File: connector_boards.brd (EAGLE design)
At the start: 59.9 x 46 mm, 3 parts

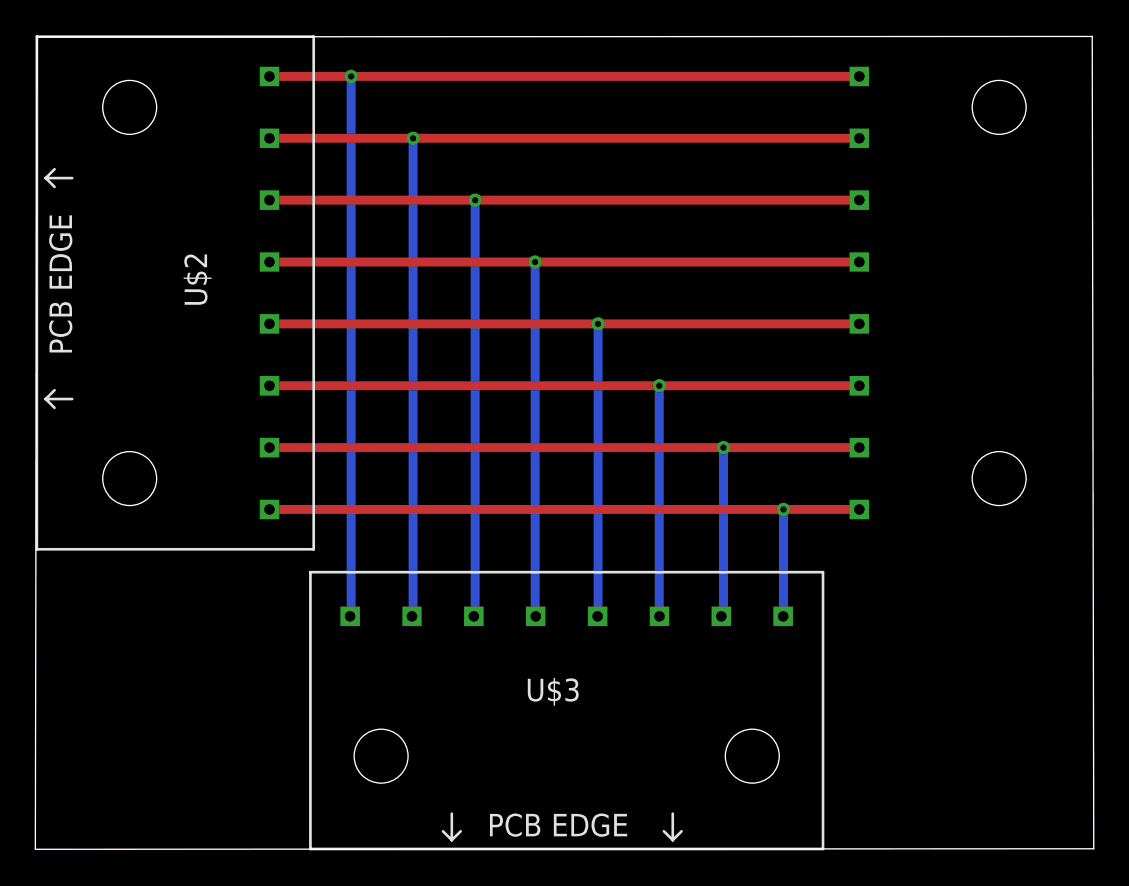
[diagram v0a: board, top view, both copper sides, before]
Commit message: Return to the original state after major disruption
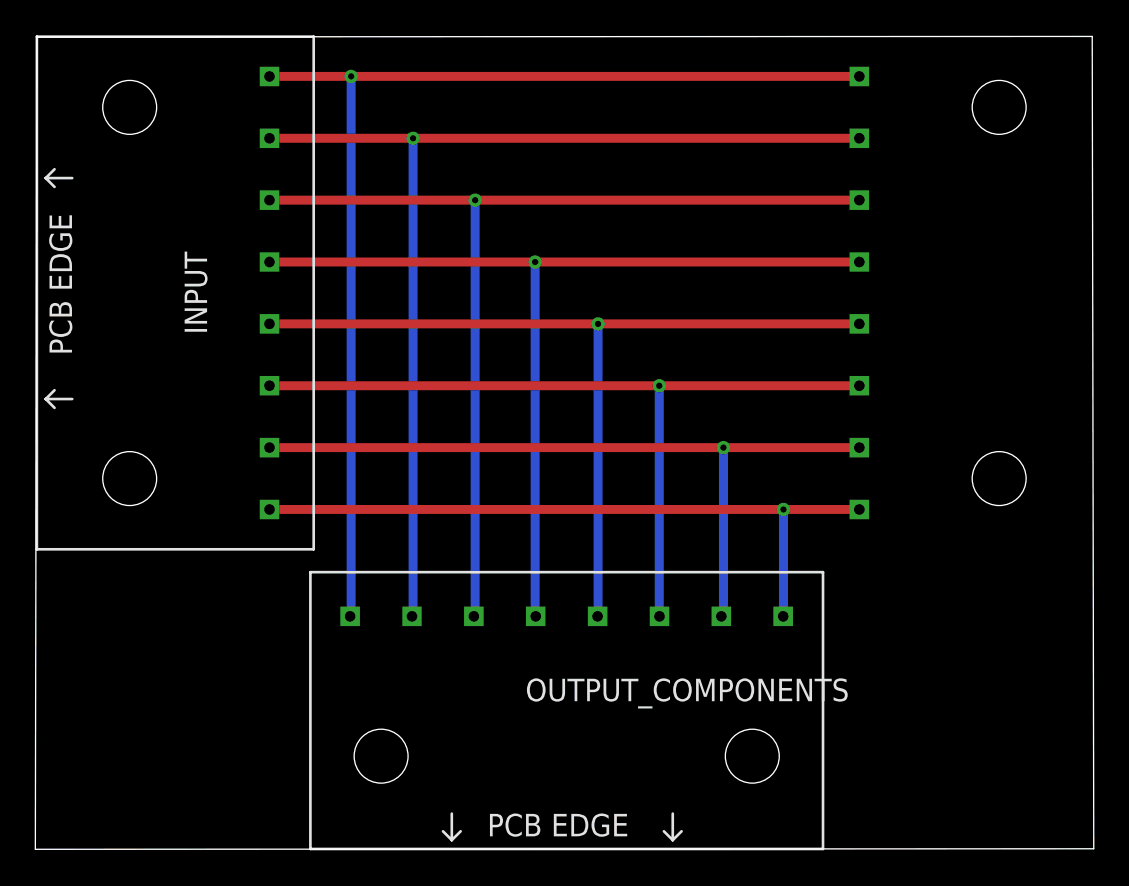
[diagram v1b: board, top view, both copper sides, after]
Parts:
- renumbered U$1 to OUTPUT, U$2 to INPUT, U$3 to OUTPUT_COMPONENTS
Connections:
- net N$1 renamed BREAK_SIG
- net N$2 renamed HAZ_L_SIG
- net N$3 renamed HAZ_R_SIG
- net N$4 renamed HEADLIGHT_SIG
- net N$5 renamed REARLIGHT_SIG
- net N$8 renamed GND
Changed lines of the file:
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@@
 <?xml version="1.0" encoding="utf-8"?>
 <!DOCTYPE eagle SYSTEM "eagle.dtd">
-<eagle version="9.1.3">
+<eagle version="9.2.2">
 <drawing>
 <settings>
@@
 </autorouter>
 <elements>
-<element name="U$1" library="master_library" package="8-PIN-MOLEX" value="8-PIN-MOLEX-RA-FEMALE" x="91.44" y="67.31" rot="MR270"/>
-<element name="U$2" library="master_library" package="8-PIN-MOLEX" value="8-PIN-MOLEX-RA-FEMALE" x="31.75" y="67.31" rot="R270"/>
-<element name="U$3" library="master_library" package="8-PIN-MOLEX" value="8-PIN-MOLEX-RA-FEMALE" x="47.224134375" y="21.35574375"/>
+<element name="OUTPUT" library="master_library" package="8-PIN-MOLEX" value="8-PIN-MOLEX-RA-FEMALE" x="91.44" y="67.31" smashed="yes" rot="MR270">
+<attribute name="NAME" x="83.080334375" y="55.148" size="1.27" layer="26" rot="MR270"/>
+</element>
+<element name="INPUT" library="master_library" package="8-PIN-MOLEX" value="8-PIN-MOLEX-RA-FEMALE" x="31.75" y="67.31" smashed="yes" rot="R270">
+<attribute name="NAME" x="40.109665625" y="55.148" size="1.27" layer="25" rot="R270"/>
+</element>
+<element name="OUTPUT_COMPONENTS" library="master_library" package="8-PIN-MOLEX" value="8-PIN-MOLEX-RA-FEMALE" x="47.224134375" y="21.35574375" smashed="yes">
+<attribute name="NAME" x="59.386134375" y="29.715409375" size="1.27" layer="25"/>
+</element>
 </elements>
 <signals>
-<signal name="N$1">
-<contactref element="U$1" pad="P1"/>
-<contactref element="U$2" pad="P1"/>
-<contactref element="U$3" pad="P1"/>
+<signal name="BREAK_SIG">
+<contactref element="OUTPUT" pad="P1"/>
+<contactref element="INPUT" pad="P1"/>
+<contactref element="OUTPUT_COMPONENTS" pad="P1"/>
 <wire x1="49.53" y1="65.062" x2="78.28" y2="65.062" width="0.508" layer="1"/>
 <wire x1="44.91" y1="65.062" x2="49.53" y2="65.062" width="0.508" layer="1"/>
@@
 <wire x1="49.53" y1="34.573609375" x2="49.472134375" y2="34.51574375" width="0.508" layer="16"/>
 </signal>
-<signal name="N$2">
-<contactref element="U$1" pad="P2"/>
-<contactref element="U$2" pad="P2"/>
-<contactref element="U$3" pad="P2"/>
+<signal name="HAZ_L_SIG">
+<contactref element="OUTPUT" pad="P2"/>
+<contactref element="INPUT" pad="P2"/>
+<contactref element="OUTPUT_COMPONENTS" pad="P2"/>
 <wire x1="53.031821875" y1="61.562" x2="78.28" y2="61.562" width="0.508" layer="1"/>
 <wire x1="44.91" y1="61.562" x2="53.031821875" y2="61.562" width="0.508" layer="1"/>
@@
 <wire x1="53.031821875" y1="34.57543125" x2="52.972134375" y2="34.51574375" width="0.508" layer="16"/>
 </signal>
-<signal name="N$3">
-<contactref element="U$1" pad="P3"/>
-<contactref element="U$2" pad="P3"/>
-<contactref element="U$3" pad="P3"/>
+<signal name="HAZ_R_SIG">
+<contactref element="OUTPUT" pad="P3"/>
+<contactref element="INPUT" pad="P3"/>
+<contactref element="OUTPUT_COMPONENTS" pad="P3"/>
 <wire x1="56.543865625" y1="58.062" x2="78.28" y2="58.062" width="0.508" layer="1"/>
 <wire x1="44.91" y1="58.062" x2="56.543865625" y2="58.062" width="0.508" layer="1"/>
@@
 <wire x1="56.543865625" y1="34.587475" x2="56.472134375" y2="34.51574375" width="0.508" layer="16"/>
 </signal>
-<signal name="N$4">
-<contactref element="U$1" pad="P4"/>
-<contactref element="U$2" pad="P4"/>
-<contactref element="U$3" pad="P4"/>
+<signal name="HEADLIGHT_SIG">
+<contactref element="OUTPUT" pad="P4"/>
+<contactref element="INPUT" pad="P4"/>
+<contactref element="OUTPUT_COMPONENTS" pad="P4"/>
 <wire x1="59.9388375" y1="54.562" x2="78.28" y2="54.562" width="0.508" layer="1"/>
 <wire x1="44.91" y1="54.562" x2="59.9388375" y2="54.562" width="0.508" layer="1"/>
@@
 <wire x1="59.9388375" y1="34.549040625" x2="59.972134375" y2="34.51574375" width="0.508" layer="16"/>
 </signal>
-<signal name="N$5">
-<contactref element="U$1" pad="P5"/>
-<contactref element="U$2" pad="P5"/>
-<contactref element="U$3" pad="P5"/>
+<signal name="REARLIGHT_SIG">
+<contactref element="OUTPUT" pad="P5"/>
+<contactref element="INPUT" pad="P5"/>
+<contactref element="OUTPUT_COMPONENTS" pad="P5"/>
 <wire x1="63.5" y1="51.062" x2="78.28" y2="51.062" width="0.508" layer="1"/>
 <wire x1="44.91" y1="51.062" x2="63.5" y2="51.062" width="0.508" layer="1"/>
@@
 </signal>
 <signal name="N$6">
-<contactref element="U$1" pad="P6"/>
-<contactref element="U$2" pad="P6"/>
-<contactref element="U$3" pad="P6"/>
+<contactref element="OUTPUT" pad="P6"/>
+<contactref element="INPUT" pad="P6"/>
+<contactref element="OUTPUT_COMPONENTS" pad="P6"/>
 <wire x1="66.962921875" y1="47.562" x2="78.28" y2="47.562" width="0.508" layer="1"/>
 <wire x1="44.91" y1="47.562" x2="66.962921875" y2="47.562" width="0.508" layer="1"/>
@@
 </signal>
 <signal name="N$7">
-<contactref element="U$1" pad="P7"/>
-<contactref element="U$2" pad="P7"/>
-<contactref element="U$3" pad="P7"/>
+<contactref element="OUTPUT" pad="P7"/>
+<contactref element="INPUT" pad="P7"/>
+<contactref element="OUTPUT_COMPONENTS" pad="P7"/>
 <wire x1="70.59203125" y1="44.062" x2="78.28" y2="44.062" width="0.508" layer="1"/>
 <wire x1="44.91" y1="44.062" x2="70.59203125" y2="44.062" width="0.508" layer="1"/>
@@
 <wire x1="70.59203125" y1="34.635640625" x2="70.472134375" y2="34.51574375" width="0.508" layer="16"/>
 </signal>
-<signal name="N$8">
-<contactref element="U$1" pad="P8"/>
-<contactref element="U$2" pad="P8"/>
-<contactref element="U$3" pad="P8"/>
+<signal name="GND">
+<contactref element="OUTPUT" pad="P8"/>
+<contactref element="INPUT" pad="P8"/>
+<contactref element="OUTPUT_COMPONENTS" pad="P8"/>
 <wire x1="73.987003125" y1="40.562" x2="78.28" y2="40.562" width="0.508" layer="1"/>
 <wire x1="44.91" y1="40.562" x2="73.987003125" y2="40.562" width="0.508" layer="1"/>
